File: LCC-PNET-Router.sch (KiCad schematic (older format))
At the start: 3 parts, among them P1 POCKETBEAGLE-P1, P2 POCKETBEAGLE-P2

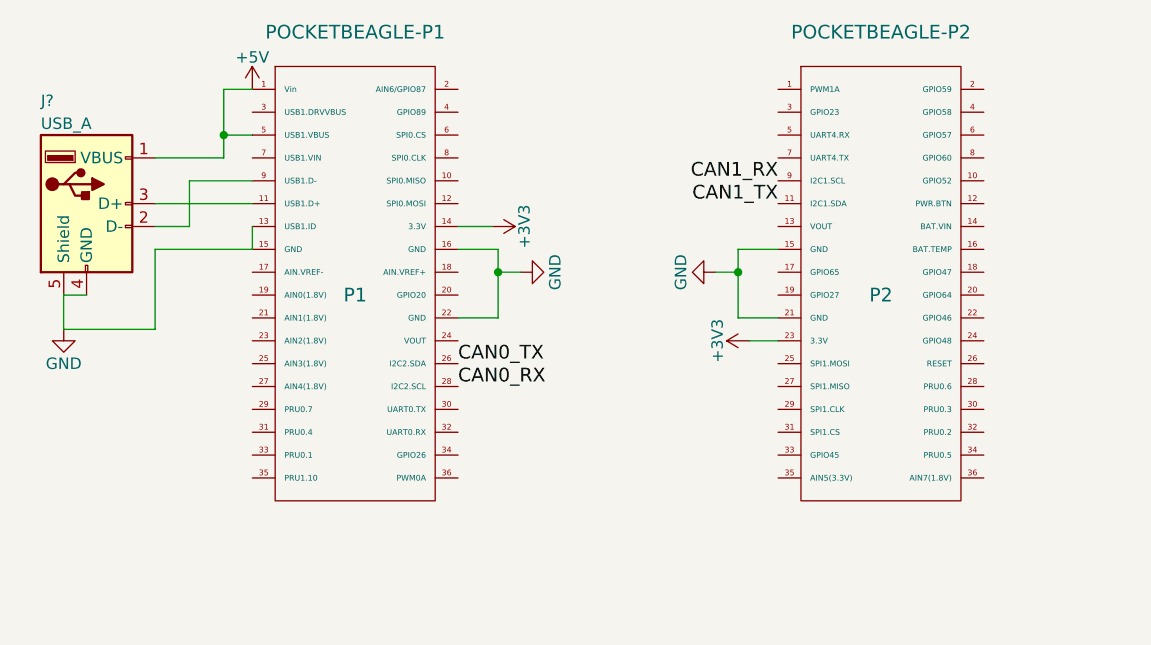
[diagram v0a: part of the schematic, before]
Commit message: Start on LCC <=> PNET router.
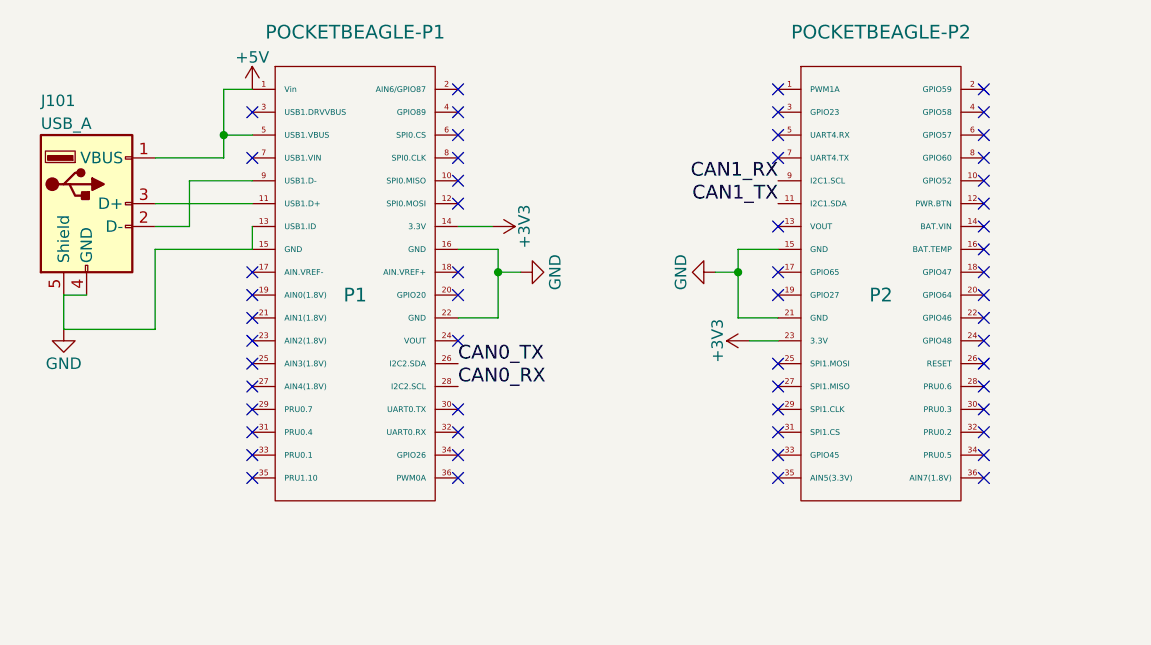
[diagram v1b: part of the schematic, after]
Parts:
- gave numbers to parts that had none: 1
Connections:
- no-connect marks 0 -> 56
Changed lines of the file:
@@
 CAN_12V
 $Comp
-L +5V #PWR?
+L +5V #PWR01
 U 1 1 63C08525
 P 7500 4225
-F 0 "#PWR?" H 7500 4075 50  0001 C CNN
+F 0 "#PWR01" H 7500 4075 50  0001 C CNN
 F 1 "+5V" H 7500 4365 50  0000 C CNN
 F 2 "" H 7500 4225 50  0001 C CNN
@@
 	7575 4225 7500 4225
 $Comp
-L +5V #PWR?
+L +5V #PWR02
 U 1 1 63C0874C
 P 2400 1650
-F 0 "#PWR?" H 2400 1500 50  0001 C CNN
+F 0 "#PWR02" H 2400 1500 50  0001 C CNN
 F 1 "+5V" H 2400 1790 50  0000 C CNN
 F 2 "" H 2400 1650 50  0001 C CNN
@@
 	2275 1850 2400 1850
 $Comp
-L USB_A J?
+L USB_A J101
 U 1 1 63C087AA
 P 1675 2150
-F 0 "J?" H 1475 2600 50  0000 L CNN
+F 0 "J101" H 1475 2600 50  0000 L CNN
 F 1 "USB_A" H 1475 2500 50  0000 L CNN
 F 2 "" H 1825 2100 50  0001 C CNN
@@
 	2400 2250 2400 2350
 $Comp
-L GND #PWR?
+L GND #PWR03
 U 1 1 63C08982
 P 1575 2700
-F 0 "#PWR?" H 1575 2450 50  0001 C CNN
+F 0 "#PWR03" H 1575 2450 50  0001 C CNN
 F 1 "GND" H 1575 2550 50  0000 C CNN
 F 2 "" H 1575 2700 50  0001 C CNN
@@
 	1975 2700 1575 2700
 $Comp
-L +3V3 #PWR?
+L +3V3 #PWR04
 U 1 1 63C08B7C
 P 3450 2250
-F 0 "#PWR?" H 3450 2100 50  0001 C CNN
+F 0 "#PWR04" H 3450 2100 50  0001 C CNN
 F 1 "+3V3" H 3450 2390 50  0000 C CNN
 F 2 "" H 3450 2250 50  0001 C CNN
@@
 	3450 2250 3300 2250
 $Comp
-L +3V3 #PWR?
+L +3V3 #PWR05
 U 1 1 63C08EDB
 P 4575 2750
-F 0 "#PWR?" H 4575 2600 50  0001 C CNN
+F 0 "#PWR05" H 4575 2600 50  0001 C CNN
 F 1 "+3V3" H 4575 2890 50  0000 C CNN
 F 2 "" H 4575 2750 50  0001 C CNN
@@
 	3475 2650 3300 2650
 $Comp
-L GND #PWR?
+L GND #PWR06
 U 1 1 63C08FA9
 P 4425 2450
-F 0 "#PWR?" H 4425 2200 50  0001 C CNN
+F 0 "#PWR06" H 4425 2200 50  0001 C CNN
 F 1 "GND" H 4425 2300 50  0000 C CNN
 F 2 "" H 4425 2450 50  0001 C CNN
@@
 Connection ~ 4525 2450
 $Comp
-L GND #PWR?
+L GND #PWR07
 U 1 1 63C09020
 P 3575 2450
-F 0 "#PWR?" H 3575 2200 50  0001 C CNN
+F 0 "#PWR07" H 3575 2200 50  0001 C CNN
 F 1 "GND" H 3575 2300 50  0000 C CNN
 F 2 "" H 3575 2450 50  0001 C CNN
@@
 Text Label 4375 4575 2    60   ~ 0
 CAN1_RX
+NoConn ~ 2400 1750
+NoConn ~ 2400 1950
+NoConn ~ 2400 2450
+NoConn ~ 2400 2550
+NoConn ~ 2400 2650
+NoConn ~ 2400 2750
+NoConn ~ 2400 2850
+NoConn ~ 2400 2950
+NoConn ~ 2400 3050
+NoConn ~ 2400 3150
+NoConn ~ 2400 3250
+NoConn ~ 2400 3350
+NoConn ~ 3300 3350
+NoConn ~ 4700 3350
+NoConn ~ 4700 3250
+NoConn ~ 4700 3150
+NoConn ~ 4700 3050
+NoConn ~ 4700 2950
+NoConn ~ 3300 3050
+NoConn ~ 3300 3150
+NoConn ~ 3300 3250
+NoConn ~ 4700 2850
+NoConn ~ 3300 2750
+NoConn ~ 4700 2550
+NoConn ~ 4700 2450
+NoConn ~ 3300 2450
+NoConn ~ 3300 2550
+NoConn ~ 4700 1650
+NoConn ~ 4700 1750
+NoConn ~ 4700 1850
+NoConn ~ 4700 1950
+NoConn ~ 4700 2250
+NoConn ~ 3300 1650
+NoConn ~ 3300 1750
+NoConn ~ 3300 1850
+NoConn ~ 3300 1950
+NoConn ~ 3300 2050
+NoConn ~ 3300 2150
+NoConn ~ 5600 1650
+NoConn ~ 5600 1750
+NoConn ~ 5600 1850
+NoConn ~ 5600 1950
+NoConn ~ 5600 2050
+NoConn ~ 5600 2150
+NoConn ~ 5600 2250
+NoConn ~ 5600 2350
+NoConn ~ 5600 2450
+NoConn ~ 5600 2550
+NoConn ~ 5600 2650
+NoConn ~ 5600 2750
+NoConn ~ 5600 2850
+NoConn ~ 5600 2950
+NoConn ~ 5600 3050
+NoConn ~ 5600 3150
+NoConn ~ 5600 3250
+NoConn ~ 5600 3350
 $EndSCHEMATC

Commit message: Start on PCB layout.
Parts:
- J101: footprint (none) -> USB-A-Upright:USB-A-UPRIGHT; Mouser Part Number (none) -> 710-614004184726
- P1, P2: footprint (none) -> Socket_Strips:Socket_Strip_Straight_2x18_Pitch2.54mm
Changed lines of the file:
@@
 F 0 "P1" H 2850 2550 60  0000 C CNN
 F 1 "POCKETBEAGLE-P1" H 2850 3700 60  0000 C CNN
-F 2 "" H 2850 2550 60  0000 C CNN
+F 2 "Socket_Strips:Socket_Strip_Straight_2x18_Pitch2.54mm" H 2850 2550 60  0001 C CNN
 F 3 "" H 2850 2550 60  0000 C CNN
 	1    2850 2550
@@
 F 0 "P2" H 5150 2550 60  0000 C CNN
 F 1 "POCKETBEAGLE-P2" H 5150 3700 60  0000 C CNN
-F 2 "" H 5150 2550 60  0000 C CNN
+F 2 "Socket_Strips:Socket_Strip_Straight_2x18_Pitch2.54mm" H 5150 2550 60  0001 C CNN
 F 3 "" H 5150 2550 60  0000 C CNN
 	1    5150 2550
@@
 F 0 "J101" H 1475 2600 50  0000 L CNN
 F 1 "USB_A" H 1475 2500 50  0000 L CNN
-F 2 "" H 1825 2100 50  0001 C CNN
+F 2 "USB-A-Upright:USB-A-UPRIGHT" H 1825 2100 50  0001 C CNN
 F 3 "" H 1825 2100 50  0001 C CNN
+F 4 "710-614004184726" H 1675 2150 60  0001 C CNN "Mouser Part Number"
 	1    1675 2150
 	1    0    0    -1
